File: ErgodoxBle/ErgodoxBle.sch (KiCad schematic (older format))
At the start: 82 parts, among them K0 KEYSW, K1 KEYSW, K10 KEYSW, K11 KEYSW, K12 KEYSW, K13 KEYSW, K14 KEYSW, K15 KEYSW, K16 KEYSW, K2 KEYSW, K20 KEYSW, K21 KEYSW, K22 KEYSW, K23 KEYSW, K24 KEYSW, K25 KEYSW, K26 KEYSW, K3 KEYSW, K30 KEYSW, K31 KEYSW, K32 KEYSW, K33 KEYSW, K34 KEYSW, K35 KEYSW, K36 KEYSW, K4 KEYSW, K40 KEYSW, K41 KEYSW, K42 KEYSW, K43 KEYSW, K44 KEYSW, K45 KEYSW, K46 KEYSW, K5 KEYSW, K54 KEYSW, K55 KEYSW, K56 KEYSW, K6 KEYSW

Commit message: finish prototype
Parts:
- added SW1, SW2: SW_PUSH, Button_Switch_SMD:SW_SPST_TL3342, symbol keyboard_parts2:SW_PUSH
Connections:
- net GND: now also SW1.2, SW2.2
- net RST: now reaches MCU1.22 (RST)
- net RST: now also SW1.1, SW2.1
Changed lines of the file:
@@
 Text GLabel 1350 3850 2    50   Input ~ 0
 scl
-Text GLabel 1350 3750 2    50   Input ~ 0
-GND
-Text GLabel 1200 4750 2    50   Input ~ 0
-GND
 Text GLabel 1200 4850 2    50   Input ~ 0
 scl
@@
 Text GLabel 1800 6300 2    50   Input ~ 0
 Vcc
-Text GLabel 2200 850  2    50   Input ~ 0
-GND
 Text GLabel 2200 1050 2    50   Input ~ 0
 Vcc
-Text GLabel 800  950  0    50   Input ~ 0
-GND
-Text GLabel 800  1050 0    50   Input ~ 0
-GND
+Text GLabel 2200 950  2    50   Input ~ 0
+RST
+$Comp
+L keyboard_parts2:SW_PUSH SW1
+U 1 1 5C4487C0
+P 3250 6250
+F 0 "SW1" H 3250 6505 50  0000 C CNN
+F 1 "SW_PUSH" H 3250 6414 50  0000 C CNN
+F 2 "Button_Switch_SMD:SW_SPST_TL3342" H 3250 6250 60  0001 C CNN
+F 3 "" H 3250 6250 60  0000 C CNN
+	1    3250 6250
+	1    0    0    -1
+$EndComp
+$Comp
+L keyboard_parts2:SW_PUSH SW2
+U 1 1 5C448928
+P 3250 6650
+F 0 "SW2" H 3250 6905 50  0000 C CNN
+F 1 "SW_PUSH" H 3250 6814 50  0000 C CNN
+F 2 "Button_Switch_SMD:SW_SPST_TL3342" H 3250 6650 60  0001 C CNN
+F 3 "" H 3250 6650 60  0000 C CNN
+	1    3250 6650
+	1    0    0    -1
+$EndComp
+Wire Wire Line
+	2350 6450 2850 6450
+Wire Wire Line
+	2850 6450 2850 6250
+Wire Wire Line
+	2850 6250 2950 6250
+Wire Wire Line
+	2850 6450 2850 6650
+Wire Wire Line
+	2850 6650 2950 6650
+Connection ~ 2850 6450
+Wire Wire Line
+	3550 6250 3750 6250
+Wire Wire Line
+	3750 6250 3750 6450
+Wire Wire Line
+	3750 6650 3550 6650
+Wire Wire Line
+	3750 6450 4200 6450
+Connection ~ 3750 6450
+Wire Wire Line
+	3750 6450 3750 6650
+Text GLabel 2350 6450 0    50   Input ~ 0
+RST
+$Comp
+L power:GND #PWR0101
+U 1 1 5C486B80
+P 4200 6450
+F 0 "#PWR0101" H 4200 6200 50  0001 C CNN
+F 1 "GND" V 4205 6322 50  0000 R CNN
+F 2 "" H 4200 6450 50  0001 C CNN
+F 3 "" H 4200 6450 50  0001 C CNN
+	1    4200 6450
+	0    -1   -1   0
+$EndComp
+$Comp
+L power:GND #PWR0102
+U 1 1 5C49D3FD
+P 800 950
+F 0 "#PWR0102" H 800 700 50  0001 C CNN
+F 1 "GND" V 805 822 50  0000 R CNN
+F 2 "" H 800 950 50  0001 C CNN
+F 3 "" H 800 950 50  0001 C CNN
+	1    800  950
+	0    1    1    0
+$EndComp
+$Comp
+L power:GND #PWR0103
+U 1 1 5C49D51B
+P 800 1050
+F 0 "#PWR0103" H 800 800 50  0001 C CNN
+F 1 "GND" V 805 922 50  0000 R CNN
+F 2 "" H 800 1050 50  0001 C CNN
+F 3 "" H 800 1050 50  0001 C CNN
+	1    800  1050
+	0    1    1    0
+$EndComp
+$Comp
+L power:GND #PWR0104
+U 1 1 5C49D694
+P 2200 850
+F 0 "#PWR0104" H 2200 600 50  0001 C CNN
+F 1 "GND" V 2205 722 50  0000 R CNN
+F 2 "" H 2200 850 50  0001 C CNN
+F 3 "" H 2200 850 50  0001 C CNN
+	1    2200 850
+	0    -1   -1   0
+$EndComp
+$Comp
+L power:GND #PWR0105
+U 1 1 5C49E86E
+P 1350 3750
+F 0 "#PWR0105" H 1350 3500 50  0001 C CNN
+F 1 "GND" V 1355 3622 50  0000 R CNN
+F 2 "" H 1350 3750 50  0001 C CNN
+F 3 "" H 1350 3750 50  0001 C CNN
+	1    1350 3750
+	0    -1   -1   0
+$EndComp
+$Comp
+L power:GND #PWR0106
+U 1 1 5C4A6C0C
+P 1200 4750
+F 0 "#PWR0106" H 1200 4500 50  0001 C CNN
+F 1 "GND" V 1205 4622 50  0000 R CNN
+F 2 "" H 1200 4750 50  0001 C CNN
+F 3 "" H 1200 4750 50  0001 C CNN
+	1    1200 4750
+	0    -1   -1   0
+$EndComp
 $EndSCHEMATC

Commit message: use correct switch footprint
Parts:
- K0, K1, K10, K11, K12, K13, K14, K15, K16, K2, K20, K21, K22, K23, K24, K25, K26, K3, K30, K31, K32, K33, K34, K35, K36, K4, K40, K41, K42, K43, K44, K45, K46, K5, K56, K6: footprint Keebio-Parts:Hybrid_PCB_100H_Dual_hole -> footprints:Mx_Alps_100-dualside
- K54, K55: footprint Keebio-Parts:Hybrid_PCB_200H-dual -> footprints:Mx_Alps_200-dualside

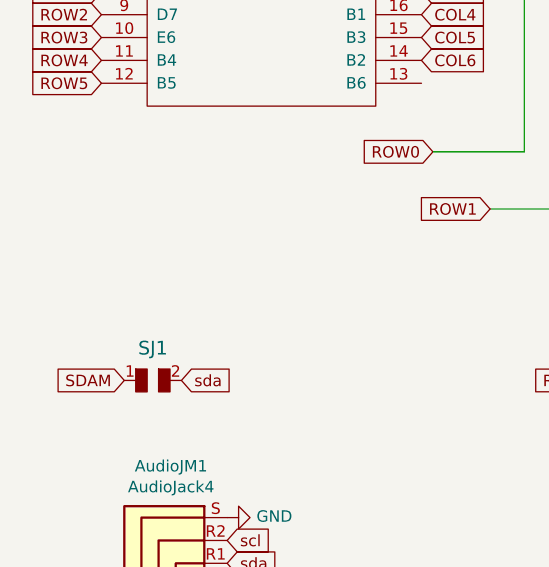
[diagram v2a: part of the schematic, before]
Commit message: add solder jumpber on both layers
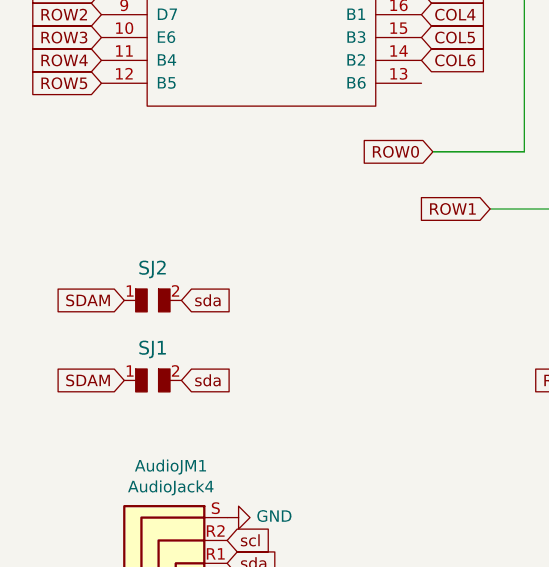
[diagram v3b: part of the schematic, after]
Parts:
- added SJ2: SOLDER_JUMPER, Keebio-Parts:solder_jumper, symbol keyboard_parts:SOLDER_JUMPER
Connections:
- net SDAM: now also SJ2.1
- net sda: now also SJ2.2
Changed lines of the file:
@@
 	0    -1   -1   0
 $EndComp
+$Comp
+L keyboard_parts:SOLDER_JUMPER SJ2
+U 1 1 5C44C788
+P 1000 2850
+F 0 "SJ2" H 1025 3041 60  0000 C CNN
+F 1 "SOLDER_JUMPER" H 1050 3000 60  0001 C CNN
+F 2 "Keebio-Parts:solder_jumper" H 1050 2850 60  0001 C CNN
+F 3 "" H 1050 2850 60  0000 C CNN
+	1    1000 2850
+	1    0    0    -1
+$EndComp
+Text GLabel 1150 2800 2    50   Input ~ 0
+sda
+Text GLabel 900  2800 0    50   Input ~ 0
+SDAM
 $EndSCHEMATC

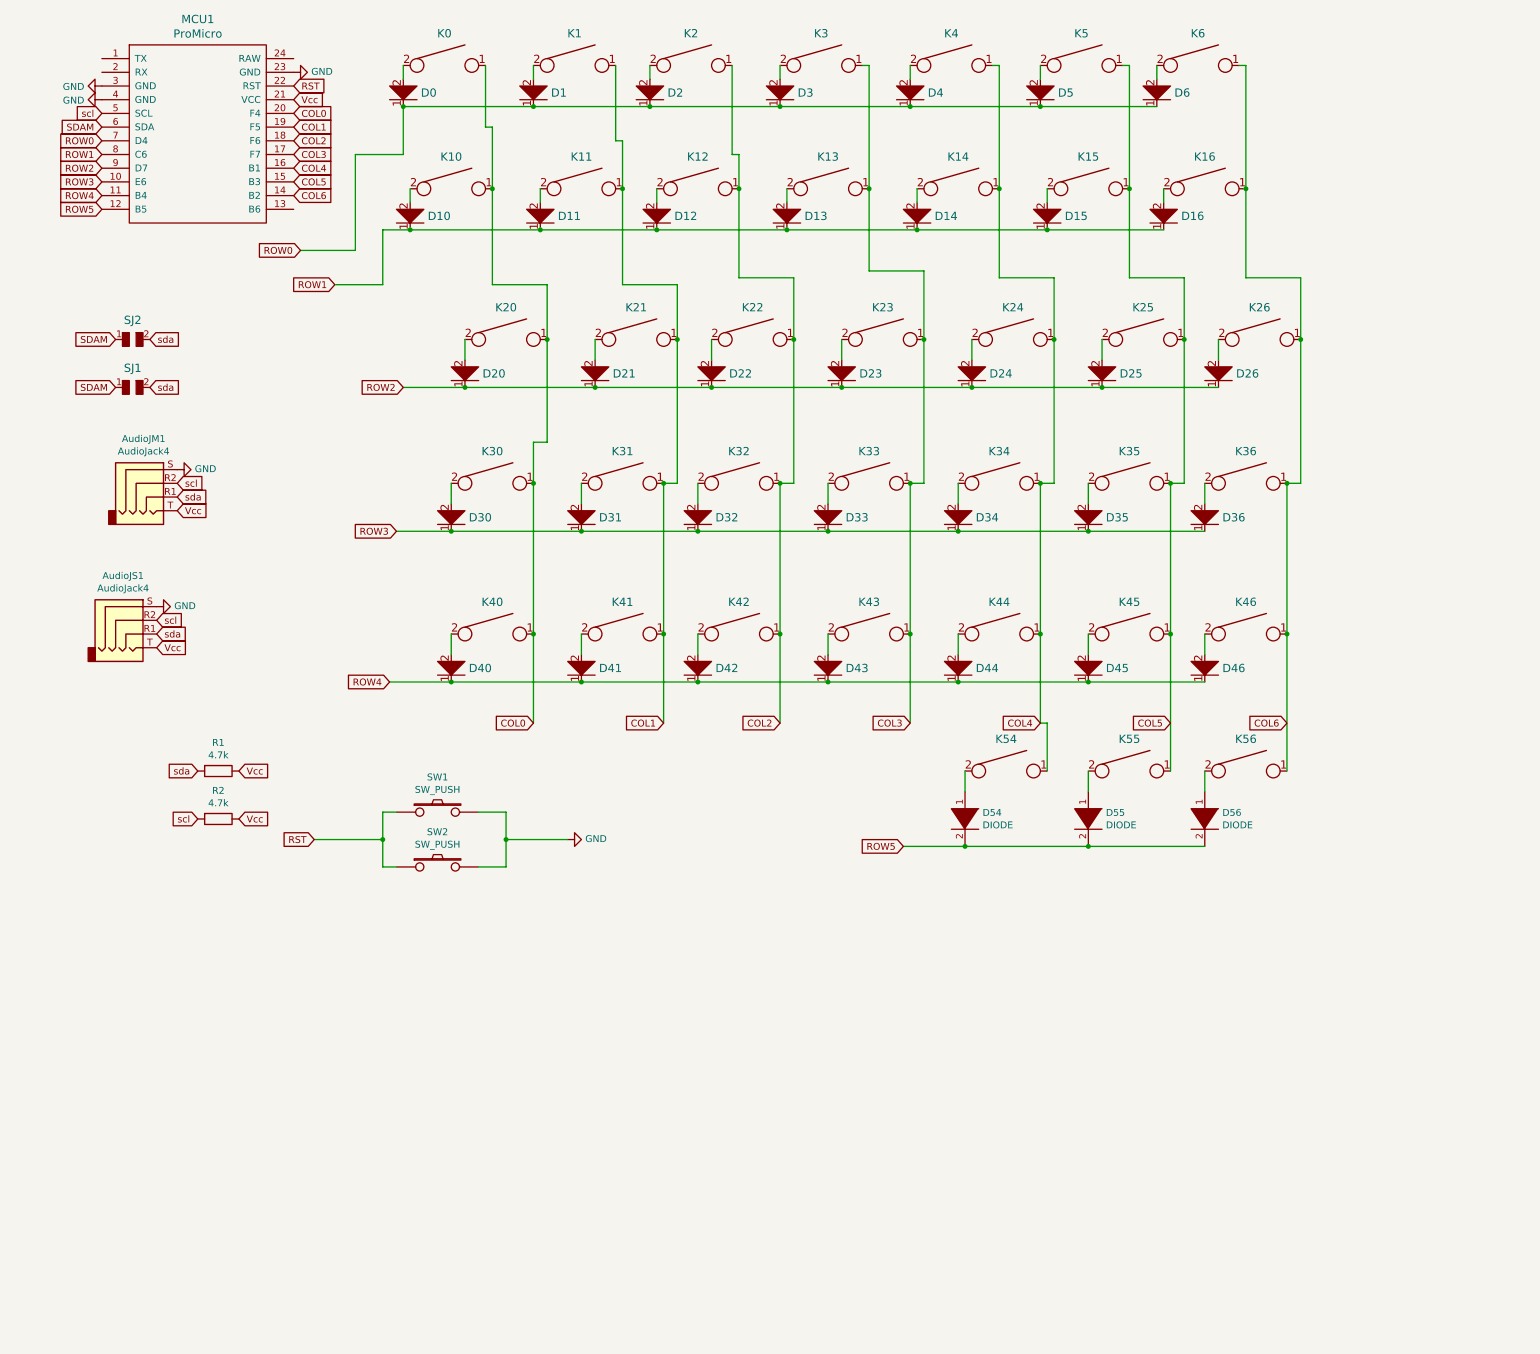
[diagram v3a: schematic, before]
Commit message: added clearence for ProtonC
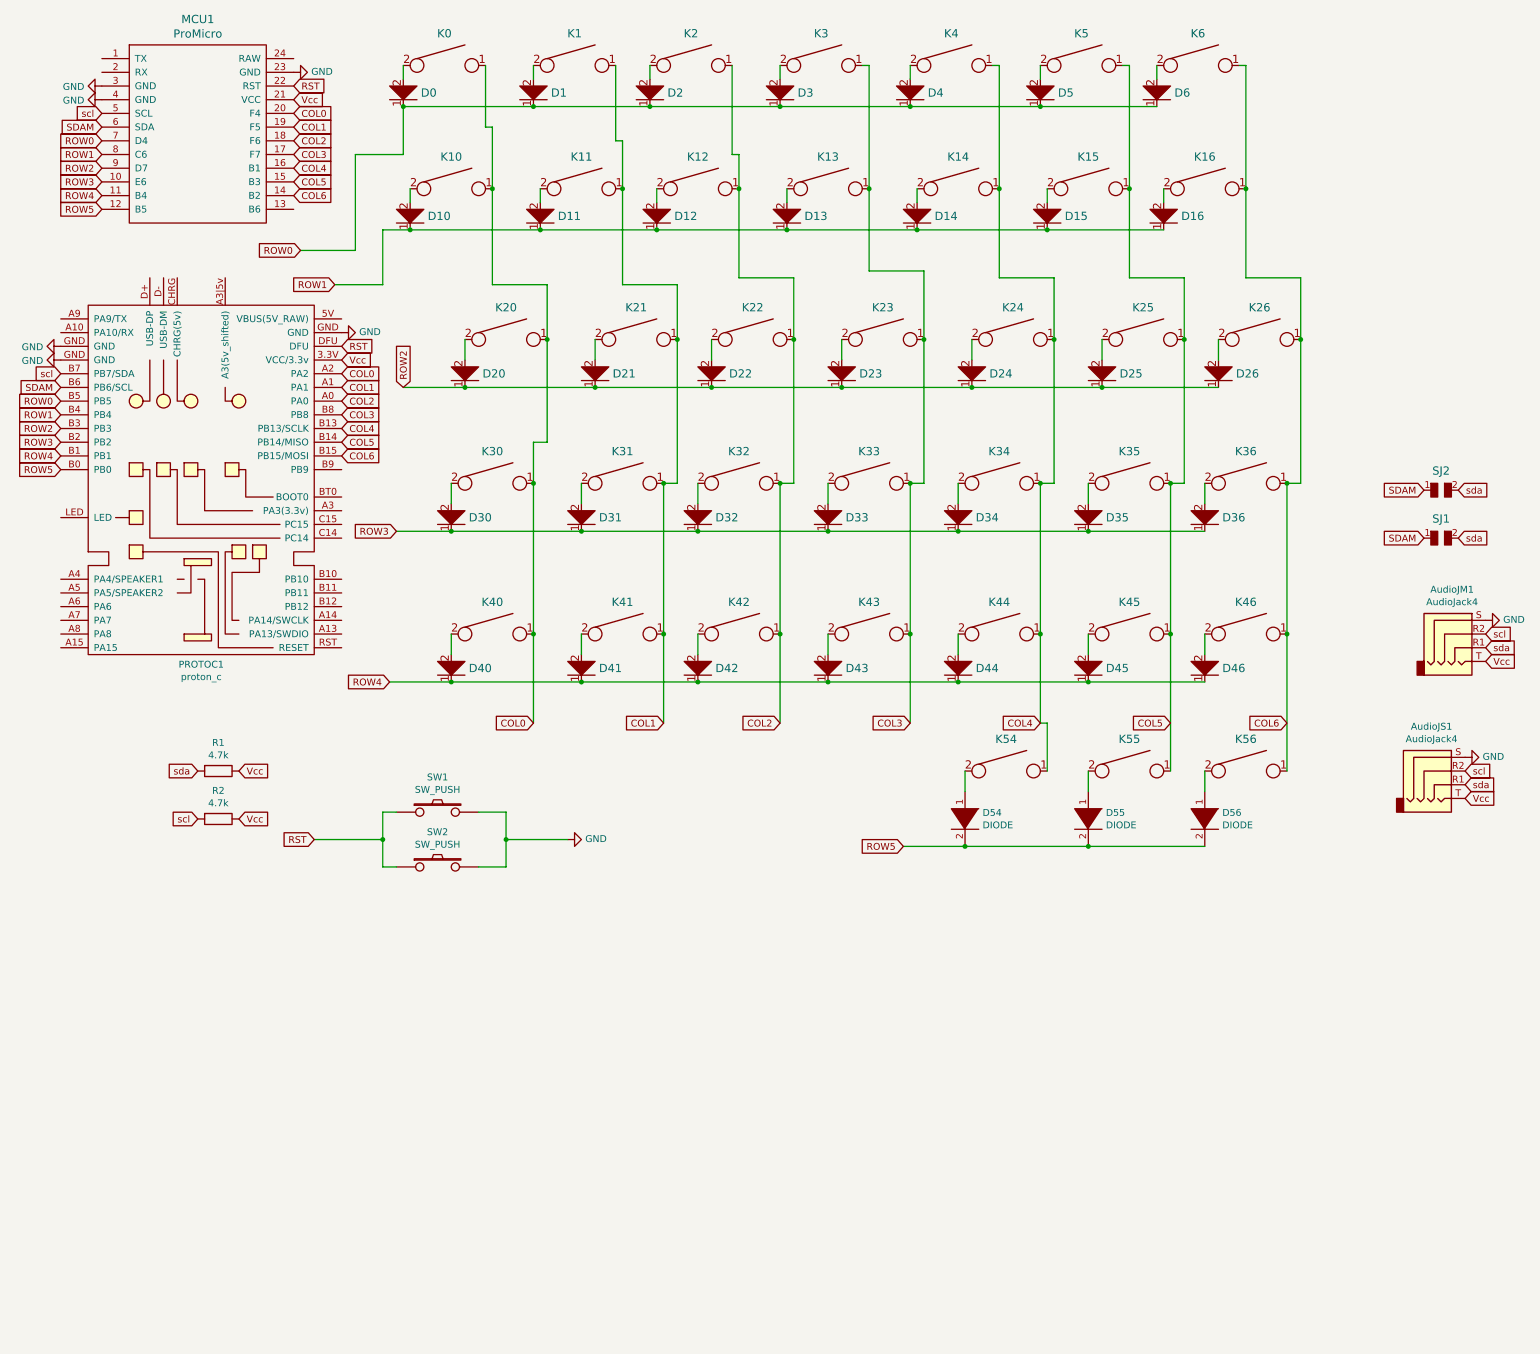
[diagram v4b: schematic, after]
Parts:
- added PROTOC1: proton_c, protonc:proton_c, symbol proton_c:proton_c
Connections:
- net COL0: now also PROTOC1.A2 (PA2)
- net COL1: now also PROTOC1.A1 (PA1)
- net COL2: now also PROTOC1.A0 (PA0)
- net COL3: now also PROTOC1.B8 (PB8)
- net COL4: now also PROTOC1.B13 (PB13/SCLK)
- net COL5: now also PROTOC1.B14 (PB14/MISO)
- net COL6: now also PROTOC1.B15 (PB15/MOSI)
- net GND: now also PROTOC1.GND
- net ROW0: now also PROTOC1.B5 (PB5)
- net ROW1: now also PROTOC1.B4 (PB4)
- net ROW2: now also PROTOC1.B3 (PB3)
- net ROW3: now also PROTOC1.B2 (PB2)
- net ROW4: now also PROTOC1.B1 (PB1)
- net ROW5: now also PROTOC1.B0 (PB0)
- net RST: now also PROTOC1.DFU
- net SDAM: now also PROTOC1.B6 (PB6/SCL)
- net Vcc: now also PROTOC1.3.3V (VCC/3.3v)
- net scl: now also PROTOC1.B7 (PB7/SDA)
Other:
- moved on the sheet: AudioJM1, AudioJS1, SJ1, SJ2
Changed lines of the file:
@@
 Text GLabel 2500 2400 0    50   Input ~ 0
 ROW1
-Text GLabel 3000 3150 0    50   Input ~ 0
+Text GLabel 3000 3150 1    50   Input ~ 0
 ROW2
 Text GLabel 2950 4200 0    50   Input ~ 0
@@
 L keyboard_parts:SOLDER_JUMPER SJ1
 U 1 1 5C479C99
-P 1000 3200
-F 0 "SJ1" H 1025 3391 60  0000 C CNN
-F 1 "SOLDER_JUMPER" H 1050 3350 60  0001 C CNN
-F 2 "Keebio-Parts:solder_jumper" H 1050 3200 60  0001 C CNN
-F 3 "" H 1050 3200 60  0000 C CNN
-	1    1000 3200
+P 10550 4300
+F 0 "SJ1" H 10575 4491 60  0000 C CNN
+F 1 "SOLDER_JUMPER" H 10600 4450 60  0001 C CNN
+F 2 "Keebio-Parts:solder_jumper" H 10600 4300 60  0001 C CNN
+F 3 "" H 10600 4300 60  0000 C CNN
+	1    10550 4300
 	1    0    0    -1
 $EndComp
@@
 L Connector:AudioJack4 AudioJM1
 U 1 1 5C4AE6FE
-P 1150 3850
-F 0 "AudioJM1" H 1105 4175 50  0000 C CNN
-F 1 "AudioJack4" H 1105 4084 50  0000 C CNN
-F 2 "Connector_Audio:Jack_3.5mm_PJ320D_Horizontal" H 1150 3850 50  0001 C CNN
-F 3 "~" H 1150 3850 50  0001 C CNN
-	1    1150 3850
+P 10700 4950
+F 0 "AudioJM1" H 10655 5275 50  0000 C CNN
+F 1 "AudioJack4" H 10655 5184 50  0000 C CNN
+F 2 "Connector_Audio:Jack_3.5mm_PJ320D_Horizontal" H 10700 4950 50  0001 C CNN
+F 3 "~" H 10700 4950 50  0001 C CNN
+	1    10700 4950
 	1    0    0    -1
 $EndComp
@@
 L Connector:AudioJack4 AudioJS1
 U 1 1 5C4AE81C
-P 1000 4850
-F 0 "AudioJS1" H 955 5175 50  0000 C CNN
-F 1 "AudioJack4" H 955 5084 50  0000 C CNN
-F 2 "Connector_Audio:Jack_3.5mm_PJ320D_Horizontal" H 1000 4850 50  0001 C CNN
-F 3 "~" H 1000 4850 50  0001 C CNN
-	1    1000 4850
-	1    0    0    -1
-$EndComp
-Text GLabel 1350 4050 2    50   Input ~ 0
-Vcc
-Text GLabel 1350 3950 2    50   Input ~ 0
+P 10550 5950
+F 0 "AudioJS1" H 10505 6275 50  0000 C CNN
+F 1 "AudioJack4" H 10505 6184 50  0000 C CNN
+F 2 "Connector_Audio:Jack_3.5mm_PJ320D_Horizontal" H 10550 5950 50  0001 C CNN
+F 3 "~" H 10550 5950 50  0001 C CNN
+	1    10550 5950
+	1    0    0    -1
+$EndComp
+Text GLabel 10900 5150 2    50   Input ~ 0
+Vcc
+Text GLabel 10900 5050 2    50   Input ~ 0
 sda
-Text GLabel 1350 3850 2    50   Input ~ 0
+Text GLabel 10900 4950 2    50   Input ~ 0
 scl
-Text GLabel 1200 4850 2    50   Input ~ 0
+Text GLabel 10750 5950 2    50   Input ~ 0
 scl
-Text GLabel 1200 4950 2    50   Input ~ 0
+Text GLabel 10750 6050 2    50   Input ~ 0
 sda
-Text GLabel 1200 5050 2    50   Input ~ 0
-Vcc
-Text GLabel 1150 3150 2    50   Input ~ 0
+Text GLabel 10750 6150 2    50   Input ~ 0
+Vcc
+Text GLabel 10700 4250 2    50   Input ~ 0
 sda
-Text GLabel 900  3150 0    50   Input ~ 0
+Text GLabel 10450 4250 0    50   Input ~ 0
 SDAM
 $Comp
@@
 L power:GND #PWR0105
 U 1 1 5C49E86E
-P 1350 3750
-F 0 "#PWR0105" H 1350 3500 50  0001 C CNN
-F 1 "GND" V 1355 3622 50  0000 R CNN
-F 2 "" H 1350 3750 50  0001 C CNN
-F 3 "" H 1350 3750 50  0001 C CNN
-	1    1350 3750
+P 10900 4850
+F 0 "#PWR0105" H 10900 4600 50  0001 C CNN
+F 1 "GND" V 10905 4722 50  0000 R CNN
+F 2 "" H 10900 4850 50  0001 C CNN
+F 3 "" H 10900 4850 50  0001 C CNN
+	1    10900 4850
 	0    -1   -1   0
 $EndComp
@@
 L power:GND #PWR0106
 U 1 1 5C4A6C0C
-P 1200 4750
-F 0 "#PWR0106" H 1200 4500 50  0001 C CNN
-F 1 "GND" V 1205 4622 50  0000 R CNN
-F 2 "" H 1200 4750 50  0001 C CNN
-F 3 "" H 1200 4750 50  0001 C CNN
-	1    1200 4750
+P 10750 5850
+F 0 "#PWR0106" H 10750 5600 50  0001 C CNN
+F 1 "GND" V 10755 5722 50  0000 R CNN
+F 2 "" H 10750 5850 50  0001 C CNN
+F 3 "" H 10750 5850 50  0001 C CNN
+	1    10750 5850
 	0    -1   -1   0
 $EndComp
@@
 L keyboard_parts:SOLDER_JUMPER SJ2
 U 1 1 5C44C788
-P 1000 2850
-F 0 "SJ2" H 1025 3041 60  0000 C CNN
-F 1 "SOLDER_JUMPER" H 1050 3000 60  0001 C CNN
-F 2 "Keebio-Parts:solder_jumper" H 1050 2850 60  0001 C CNN
-F 3 "" H 1050 2850 60  0000 C CNN
-	1    1000 2850
-	1    0    0    -1
-$EndComp
-Text GLabel 1150 2800 2    50   Input ~ 0
+P 10550 3950
+F 0 "SJ2" H 10575 4141 60  0000 C CNN
+F 1 "SOLDER_JUMPER" H 10600 4100 60  0001 C CNN
+F 2 "Keebio-Parts:solder_jumper" H 10600 3950 60  0001 C CNN
+F 3 "" H 10600 3950 60  0000 C CNN
+	1    10550 3950
+	1    0    0    -1
+$EndComp
+Text GLabel 10700 3900 2    50   Input ~ 0
 sda
-Text GLabel 900  2800 0    50   Input ~ 0
+Text GLabel 10450 3900 0    50   Input ~ 0
 SDAM
+$Comp
+L proton_c:proton_c PROTOC1
+U 1 1 5C456AFA
+P 1550 3650
+F 0 "PROTOC1" H 1525 2128 50  0000 C CNN
+F 1 "proton_c" H 1525 2037 50  0000 C CNN
+F 2 "protonc:proton_c" H 1400 3650 50  0001 C CNN
+F 3 "" H 1400 3650 50  0001 C CNN
+	1    1550 3650
+	1    0    0    -1
+$EndComp
+Text GLabel 500  3250 0    50   Input ~ 0
+ROW0
+Text GLabel 500  3350 0    50   Input ~ 0
+ROW1
+Text GLabel 500  3450 0    50   Input ~ 0
+ROW2
+Text GLabel 500  3550 0    50   Input ~ 0
+ROW3
+Text GLabel 500  3650 0    50   Input ~ 0
+ROW4
+Text GLabel 500  3750 0    50   Input ~ 0
+ROW5
+Text GLabel 2550 3050 2    50   Input ~ 0
+COL0
+Text GLabel 2550 3150 2    50   Input ~ 0
+COL1
+Text GLabel 2550 3250 2    50   Input ~ 0
+COL2
+Text GLabel 2550 3350 2    50   Input ~ 0
+COL3
+Text GLabel 2550 3450 2    50   Input ~ 0
+COL4
+Text GLabel 2550 3550 2    50   Input ~ 0
+COL5
+Text GLabel 2550 3650 2    50   Input ~ 0
+COL6
+Text GLabel 2550 2850 2    50   Input ~ 0
+RST
+Text GLabel 2550 2950 2    50   Input ~ 0
+Vcc
+Text GLabel 500  3150 0    50   Input ~ 0
+SDAM
+Text GLabel 500  3050 0    50   Input ~ 0
+scl
+$Comp
+L power:GND #PWR0107
+U 1 1 5C45843C
+P 2550 2750
+F 0 "#PWR0107" H 2550 2500 50  0001 C CNN
+F 1 "GND" V 2555 2622 50  0000 R CNN
+F 2 "" H 2550 2750 50  0001 C CNN
+F 3 "" H 2550 2750 50  0001 C CNN
+	1    2550 2750
+	0    -1   -1   0
+$EndComp
+$Comp
+L power:GND #PWR0108
+U 1 1 5C45F50C
+P 500 2850
+F 0 "#PWR0108" H 500 2600 50  0001 C CNN
+F 1 "GND" V 505 2722 50  0000 R CNN
+F 2 "" H 500 2850 50  0001 C CNN
+F 3 "" H 500 2850 50  0001 C CNN
+	1    500  2850
+	0    1    1    0
+$EndComp
+$Comp
+L power:GND #PWR0109
+U 1 1 5C47B2A2
+P 500 2950
+F 0 "#PWR0109" H 500 2700 50  0001 C CNN
+F 1 "GND" V 505 2822 50  0000 R CNN
+F 2 "" H 500 2950 50  0001 C CNN
+F 3 "" H 500 2950 50  0001 C CNN
+	1    500  2950
+	0    1    1    0
+$EndComp
 $EndSCHEMATC
